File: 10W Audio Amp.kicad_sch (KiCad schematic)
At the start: 9 parts, among them J1 AudioJack3, Q1 TIP41C, Q2 TIP42C, Q3 BD140, Q5 BD139

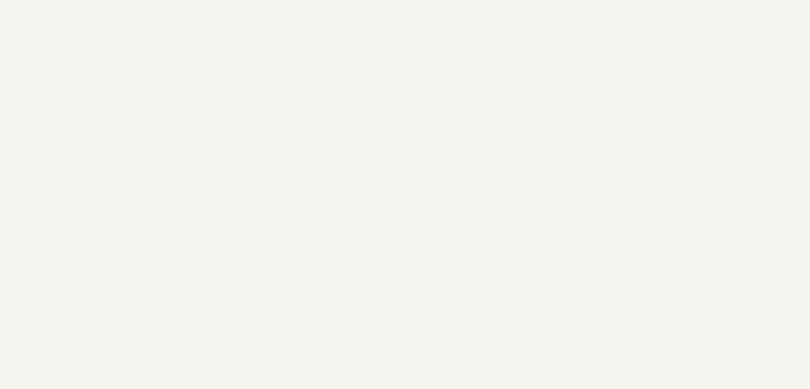
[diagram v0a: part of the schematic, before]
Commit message: Add Power supply schematic
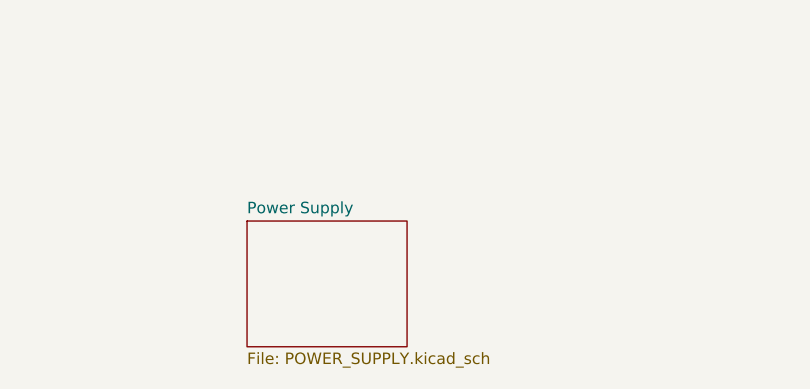
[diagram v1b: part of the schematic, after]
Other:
- added sheet Power Supply (POWER_SUPPLY.kicad_sch)
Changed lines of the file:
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@@
+		)
+	)
+	(sheet
+		(at 68.58 119.38)
+		(size 17.78 13.97)
+		(fields_autoplaced yes)
+		(stroke
+			(width 0.1524)
+			(type solid)
+		)
+		(fill
+			(color 0 0 0 0.0000)
+		)
+		(property "Sheetname" "Power Supply"
+			(at 68.58 118.6684 0)
+			(effects
+				(font
+					(size 1.27 1.27)
+				)
+				(justify left bottom)
+			)
+		)
+		(property "Sheetfile" "POWER_SUPPLY.kicad_sch"
+			(at 68.58 133.9346 0)
+			(effects
+				(font
+					(size 1.27 1.27)
+				)
+				(justify left top)
+			)
+		)
+		(instances
+			(project "10W Audio Amp"
+				(path "/653d3084-b02d-49ee-93f3-cd4dc9745562"
+					(page "2")
+				)
+			)
 		)
 	)
